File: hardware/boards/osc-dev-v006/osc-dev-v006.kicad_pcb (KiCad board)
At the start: 4 copper layers, 60 x 60 mm, 93 parts, among them J1 JST-PH-H, J10 PIN-1-3P, J11 JST-PH-V, J2 TERM, J3 PIN-1-3P, J4 PIN-2-3P, J5 JST-ZH-H, J6 PIN-1-2P, J7 PIN-1-5P, J8 PIN-2-2P, J9 PIN-1-3P, U1 HT7533-1, U2 DRV8212PDSGR, U3 CH32V006F8P6, U4 74LVC2G241

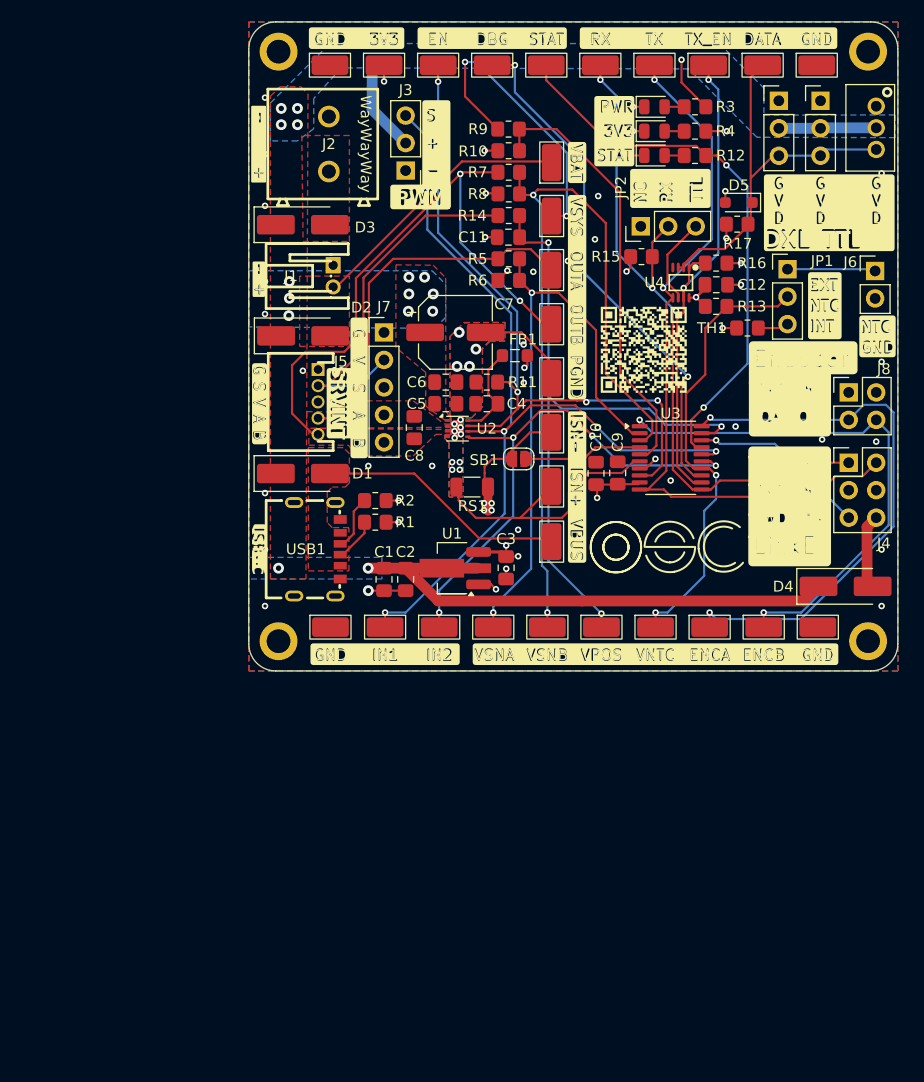
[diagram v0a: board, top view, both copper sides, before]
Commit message: hw: osc-dev-v006 rev-2a - 6l precision respin, direct-wire bus, docs
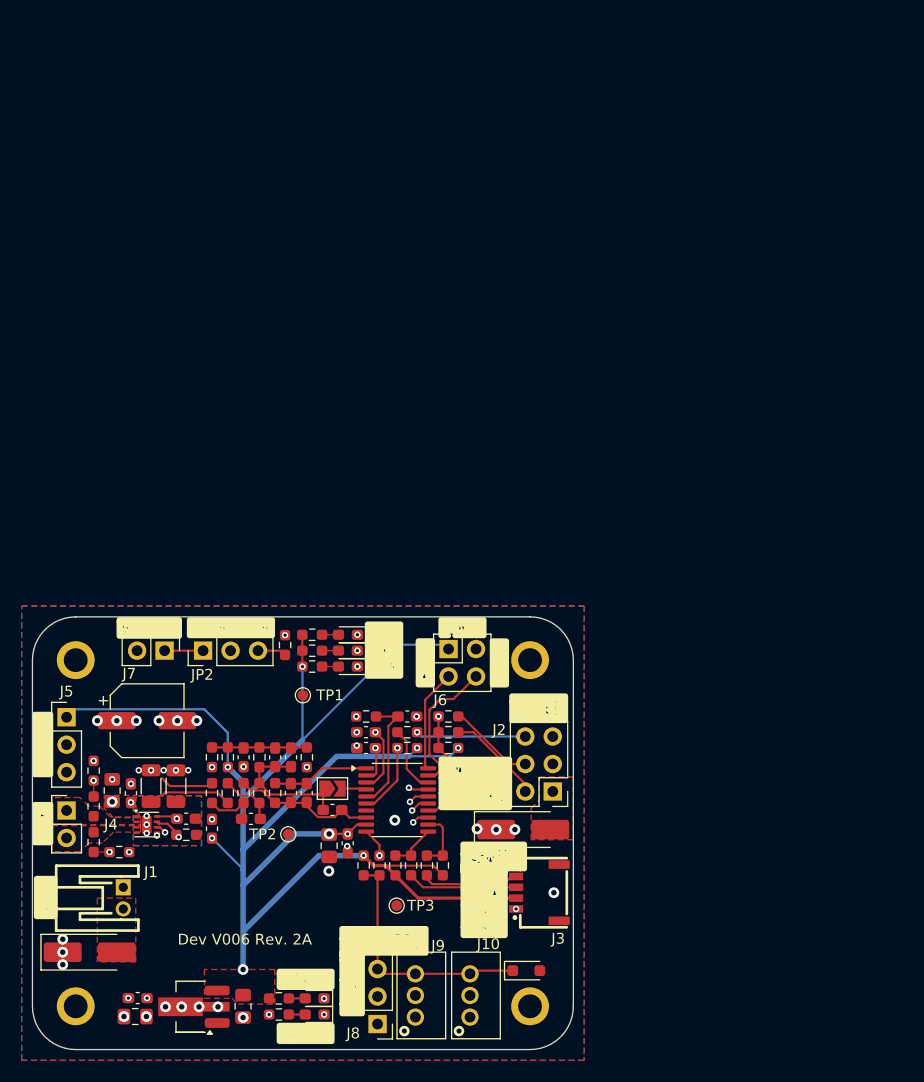
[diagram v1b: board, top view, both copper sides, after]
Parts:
- removed C10, C11, C12: 0.1µF, Capacitor_SMD:C_0805_2012Metric_Pad1.18x1.45mm_HandSolder
- removed J11: JST-PH-V, shared:CONN-TH_B3B-PH-K-S
- removed LED3: RED, LED_SMD:LED_0805_2012Metric
- removed R15, R16, R17: 10kΩ, Resistor_SMD:R_0805_2012Metric_Pad1.20x1.40mm_HandSolder
- removed SB1: Bootstrap, Jumper:SolderJumper-2_P1.3mm_Open_RoundedPad1.0x1.5mm
- removed TP10, TP11, TP12, TP13, TP14, TP15, TP16, TP17, TP18, TP19, TP20, TP21, TP22, TP23, TP24, TP25, TP26, TP27, TP28, TP4, TP5, TP6, TP7, TP8, TP9: TestPoint_Probe, TestPoint:TestPoint_Keystone_5015_Micro_Mini
- removed U4: 74LVC2G241, shared:VSSOP-8_L2.3-W2.0-P0.50-LS3.1-BR
- removed USB1: TYPE-C-H, shared:TYPE-C-SMD_TYPE-C-6P-073
- added C13: 100nF, Capacitor_SMD:C_0603_1608Metric_Pad1.08x0.95mm_HandSolder, F.Cu at (144.7, 119.2)
- added Cc1: 22pF, Capacitor_SMD:C_0603_1608Metric_Pad1.08x0.95mm_HandSolder, F.Cu at (132.4, 123.0)
- added Cc2: 22pF, Capacitor_SMD:C_0603_1608Metric_Pad1.08x0.95mm_HandSolder, F.Cu at (133.9, 126.3)
- added Cc3: 47pF, Capacitor_SMD:C_0603_1608Metric_Pad1.08x0.95mm_HandSolder, F.Cu at (133.9, 123.0)
- added Cc4: 47pF, Capacitor_SMD:C_0603_1608Metric_Pad1.08x0.95mm_HandSolder, F.Cu at (135.4, 126.3)
- added Cd1: 100nF, Capacitor_SMD:C_0603_1608Metric_Pad1.08x0.95mm_HandSolder, F.Cu at (129.5, 123.0)
- added Cin1: 100pF, Capacitor_SMD:C_0603_1608Metric_Pad1.08x0.95mm_HandSolder, F.Cu at (137.7, 127.8)
- added Ck1: 100pF, Capacitor_SMD:C_0603_1608Metric_Pad1.08x0.95mm_HandSolder, F.Cu at (130.2, 128.7)
- added Cv1: 100pF, Capacitor_SMD:C_0603_1608Metric_Pad1.08x0.95mm_HandSolder, F.Cu at (140.8, 122.1)
- added Cv2: 100pF, Capacitor_SMD:C_0603_1608Metric_Pad1.08x0.95mm_HandSolder, F.Cu at (140.8, 120.7)
- added D6: PESD5V0L1BA, Diode_SMD:D_SOD-323_HandSoldering, F.Cu at (155.7, 142.7)
- added LOGO1: osc-logo, shared:osc, F.Cu at (129.7, 136.1)
- added R21: 4K7, Resistor_SMD:R_0603_1608Metric_Pad0.98x0.95mm_HandSolder, F.Cu at (140.8, 119.2)
- added R22: 10K, Resistor_SMD:R_0603_1608Metric_Pad0.98x0.95mm_HandSolder, F.Cu at (144.7, 122.1)
- added R23: 33, Resistor_SMD:R_0603_1608Metric_Pad0.98x0.95mm_HandSolder, F.Cu at (142.1, 133.0)
- added R24: 10K, Resistor_SMD:R_0603_1608Metric_Pad0.98x0.95mm_HandSolder, F.Cu at (140.6, 133.0)
- added RS2: 60m, Resistor_SMD:R_1206_3216Metric, F.Cu at (123.3, 125.6)
- added Rd1: 1K6, Resistor_SMD:R_0603_1608Metric_Pad0.98x0.95mm_HandSolder, F.Cu at (128.1, 123.0)
- added Rd2: 300, Resistor_SMD:R_0603_1608Metric_Pad0.98x0.95mm_HandSolder, F.Cu at (126.6, 123.0)
- added Rd3: 300, Resistor_SMD:R_0603_1608Metric_Pad0.98x0.95mm_HandSolder, F.Cu at (135.4, 123.0)
- added Rf1: 6K4, Resistor_SMD:R_0603_1608Metric_Pad0.98x0.95mm_HandSolder, F.Cu at (131.0, 123.0)
- added Rf2: 6K4, Resistor_SMD:R_0603_1608Metric_Pad0.98x0.95mm_HandSolder, F.Cu at (132.4, 126.3)
- added Rg1: 430, Resistor_SMD:R_0603_1608Metric_Pad0.98x0.95mm_HandSolder, F.Cu at (131.0, 126.3)
- added Rg2: 430, Resistor_SMD:R_0603_1608Metric_Pad0.98x0.95mm_HandSolder, F.Cu at (129.5, 126.3)
- added Rk1: 0, Resistor_SMD:R_0603_1608Metric_Pad0.98x0.95mm_HandSolder, F.Cu at (128.1, 126.3)
- added Rk2: 0, Resistor_SMD:R_0603_1608Metric_Pad0.98x0.95mm_HandSolder, F.Cu at (126.6, 126.3)
- added Rv1: 20K, Resistor_SMD:R_0603_1608Metric_Pad0.98x0.95mm_HandSolder, F.Cu at (115.7, 127.5)
- added Rv2: 10K, Resistor_SMD:R_0603_1608Metric_Pad0.98x0.95mm_HandSolder, F.Cu at (115.7, 124.2)
- added Rv3: 20K, Resistor_SMD:R_0603_1608Metric_Pad0.98x0.95mm_HandSolder, F.Cu at (115.7, 130.8)
- added Rv4: 10K, Resistor_SMD:R_0603_1608Metric_Pad0.98x0.95mm_HandSolder, F.Cu at (118.0, 131.7)
- C2: footprint Capacitor_SMD:C_0805_2012Metric_Pad1.18x1.45mm_HandSolder -> Capacitor_SMD:C_0603_1608Metric_Pad1.08x0.95mm_HandSolder
- C4, C8: value 0.1µF -> 10µF
- C5: value 0.1µF -> 100nF; footprint Capacitor_SMD:C_0805_2012Metric_Pad1.18x1.45mm_HandSolder -> Capacitor_SMD:C_0603_1608Metric_Pad1.08x0.95mm_HandSolder
- C6: value 10µF -> 100nF; footprint Capacitor_SMD:C_0805_2012Metric_Pad1.18x1.45mm_HandSolder -> Capacitor_SMD:C_0603_1608Metric_Pad1.08x0.95mm_HandSolder
- C7: value 100µF -> 100nF; footprint Capacitor_SMD:CP_Elec_6.3x5.4 -> Capacitor_SMD:C_0603_1608Metric_Pad1.08x0.95mm_HandSolder
- C9: value 10µF -> 100µF; footprint Capacitor_SMD:C_0805_2012Metric_Pad1.18x1.45mm_HandSolder -> Capacitor_SMD:CP_Elec_6.3x5.4
- D3, D4: value SS54 -> BLUE; footprint Diode_SMD:D_SMA_Handsoldering -> LED_SMD:LED_0603_1608Metric_Pad1.05x0.95mm_HandSolder
- D5: value PESD5V0L1BA -> RED; footprint Diode_SMD:D_SOD-323_HandSoldering -> LED_SMD:LED_0603_1608Metric_Pad1.05x0.95mm_HandSolder
- FB1: footprint Inductor_SMD:L_0805_2012Metric_Pad1.05x1.20mm_HandSolder -> Inductor_SMD:L_0603_1608Metric_Pad1.05x0.95mm_HandSolder
- J10, J9: value PIN-1-3P -> TTL-JST; footprint Connector_PinHeader_2.54mm:PinHeader_1x03_P2.54mm_Vertical -> shared:CONN-TH_B3B-PH-K-S
- J2: value TERM -> LINKE; footprint shared:CONN-TH_2P-P5.00_WJ500V-5.08-2P -> Connector_PinHeader_2.54mm:PinHeader_2x03_P2.54mm_Vertical
- J3: value PIN-1-3P -> Qwiic; footprint Connector_PinHeader_2.54mm:PinHeader_1x03_P2.54mm_Vertical -> shared:CONN-SMD_SH1.0MM-4P-WT
- J4: value PIN-2-3P -> MOT; footprint Connector_PinHeader_2.54mm:PinHeader_2x03_P2.54mm_Vertical -> Connector_PinHeader_2.54mm:PinHeader_1x02_P2.54mm_Vertical
- J5: value JST-ZH-H -> POS; footprint shared:CONN-TH_S5B-ZR-LF-SN -> Connector_PinHeader_2.54mm:PinHeader_1x03_P2.54mm_Vertical
- J6: value PIN-1-2P -> ENC; footprint Connector_PinHeader_2.54mm:PinHeader_1x02_P2.54mm_Vertical -> Connector_PinHeader_2.54mm:PinHeader_2x02_P2.54mm_Vertical
- J7: value PIN-1-5P -> NTC; footprint Connector_PinHeader_2.54mm:PinHeader_1x05_P2.54mm_Vertical -> Connector_PinHeader_2.54mm:PinHeader_1x02_P2.54mm_Vertical
- J8: value PIN-2-2P -> TTL; footprint Connector_PinHeader_2.54mm:PinHeader_2x02_P2.54mm_Vertical -> Connector_PinHeader_2.54mm:PinHeader_1x03_P2.54mm_Vertical
- JP1: value JP-3 -> BOOTSTRAP; footprint Connector_PinHeader_2.54mm:PinHeader_1x03_P2.54mm_Vertical -> Jumper:SolderJumper-2_P1.3mm_Open_TrianglePad1.0x1.5mm
- LED1, LED2: footprint LED_SMD:LED_0805_2012Metric -> LED_SMD:LED_0603_1608Metric_Pad1.05x0.95mm_HandSolder
- R1: value 5.1kΩ -> 20K; footprint Resistor_SMD:R_0805_2012Metric_Pad1.20x1.40mm_HandSolder -> Resistor_SMD:R_0603_1608Metric_Pad0.98x0.95mm_HandSolder
- R10, R11: value 10kΩ -> 100; footprint Resistor_SMD:R_0805_2012Metric_Pad1.20x1.40mm_HandSolder -> Resistor_SMD:R_0603_1608Metric_Pad0.98x0.95mm_HandSolder
- R12: value 1kΩ -> 4K7; footprint Resistor_SMD:R_0805_2012Metric_Pad1.20x1.40mm_HandSolder -> Resistor_SMD:R_0603_1608Metric_Pad0.98x0.95mm_HandSolder
- R13, R8: value 10kΩ -> 4K7; footprint Resistor_SMD:R_0805_2012Metric_Pad1.20x1.40mm_HandSolder -> Resistor_SMD:R_0603_1608Metric_Pad0.98x0.95mm_HandSolder
- R14: value 4.7kΩ -> 10K; footprint Resistor_SMD:R_0805_2012Metric_Pad1.20x1.40mm_HandSolder -> Resistor_SMD:R_0603_1608Metric_Pad0.98x0.95mm_HandSolder
- R2: value 5.1kΩ -> 10K; footprint Resistor_SMD:R_0805_2012Metric_Pad1.20x1.40mm_HandSolder -> Resistor_SMD:R_0603_1608Metric_Pad0.98x0.95mm_HandSolder
- R3, R4: value 1.5kΩ -> 4K7; footprint Resistor_SMD:R_0805_2012Metric_Pad1.20x1.40mm_HandSolder -> Resistor_SMD:R_0603_1608Metric_Pad0.98x0.95mm_HandSolder
- R5, R7: value 20kΩ -> 100; footprint Resistor_SMD:R_0805_2012Metric_Pad1.20x1.40mm_HandSolder -> Resistor_SMD:R_0603_1608Metric_Pad0.98x0.95mm_HandSolder
- R6: value 10kΩ -> 1K; footprint Resistor_SMD:R_0805_2012Metric_Pad1.20x1.40mm_HandSolder -> Resistor_SMD:R_0603_1608Metric_Pad0.98x0.95mm_HandSolder
- R9: value 20kΩ -> 10K; footprint Resistor_SMD:R_0805_2012Metric_Pad1.20x1.40mm_HandSolder -> Resistor_SMD:R_0603_1608Metric_Pad0.98x0.95mm_HandSolder
- RS1: value 10mΩ 1% -> 33m
- TH1: footprint Resistor_SMD:R_0805_2012Metric_Pad1.20x1.40mm_HandSolder -> Resistor_SMD:R_0603_1608Metric_Pad0.98x0.95mm_HandSolder
- TP1, TP2, TP3: value TestPoint_Probe -> GND; footprint TestPoint:TestPoint_Keystone_5015_Micro_Mini -> TestPoint:TestPoint_Pad_D1.0mm
- U2: value DRV8212PDSGR -> CH32V006F8P6; footprint Package_SON:WSON-8-1EP_2x2mm_P0.5mm_EP0.9x1.6mm -> Package_SO:TSSOP-20_4.4x6.5mm_P0.65mm
- U3: value CH32V006F8P6 -> DRV8212PDSGR; footprint Package_SO:TSSOP-20_4.4x6.5mm_P0.65mm -> Package_SON:Texas_DSG0008A_WSON-8-1EP_2x2mm_P0.5mm_EP0.9x1.6mm
- moved H2 114.7 mm to (114.0, 146.0)
- moved LED1 89.6 mm to (136.1, 146.8), turned to 180 degrees
- moved J9 89.3 mm to (145.4, 145.0), turned to -90 degrees
- moved J10 88.8 mm to (150.4, 145.0), turned to -90 degrees
- moved LED2 86.1 mm to (136.1, 145.3), turned to 180 degrees
- moved J4 79.1 mm to (113.2, 127.9)
- moved J8 72.8 mm to (141.9, 147.6), turned to 180 degrees
- moved R12 69.6 mm to (147.9, 133.0), turned to -90 degrees
- moved J3 67.9 mm to (156.7, 135.5), turned to 90 degrees
- moved R10 66.5 mm to (146.5, 133.0), turned to -90 degrees
- moved R14 64.5 mm to (124.2, 130.1), turned to 0 degrees
- moved JP1 63.8 mm to (137.7, 125.9)
- moved J2 63.3 mm to (158.1, 126.1), turned to 180 degrees
- moved J1 60.7 mm to (118.4, 136.0)
- moved R3 60.3 mm to (135.9, 111.7), turned to 0 degrees
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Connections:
- C4 pad 1: /M_DRV/+3V3_DRV -> +3V3
- C4 pad 2: PGND -> GND
- C5 pad 1: VSYS -> +3V3
- C5 pad 2: PGND -> GND
- C6 pad 1: VSYS -> +3V3_DRV
- C7 pad 2: PGND -> GND
- C8 pad 1: /MOT_A -> VSYS
- C8 pad 2: /MOT_B -> GND
- C9 pad 1: +3V3 -> VSYS
- D1 pad 2: VBUS -> VBAT
- D2 pad 2: VBAT -> VPROG
- D3 pad 1: VSYS -> /MCU/TEL
- D3 pad 2: VEXT -> Net-(D3-A)
- D4 pad 1: VSYS -> /COMMS/DATA
- D4 pad 2: VPROG -> Net-(D4-A)
- D5 pad 1: /DATA -> /MCU/STAT
- D5 pad 2: GND -> Net-(D5-A)
- FB1 pad 2: /M_DRV/+3V3_DRV -> +3V3_DRV
- J10 pad 3: /DATA -> /COMMS/DATA_J
- J2 pad 1: VEXT -> VPROG
- J2 pad 2: GND -> /MCU/TEL_TX
- J3 pad 2: VSYS -> +3V3
- J3 pad 3: /IN1 -> /MCU/SDA_J
- J4 pad 1: /RX -> MOT_A
- J4 pad 2: /TX -> MOT_B
- J5 pad 1: GND -> +3V3
- J5 pad 2: /SERVO_IO/POT -> GND
- J5 pad 3: +3V3 -> /SENS/POT
- J6 pad 1: /SERVO_IO/VNTC_EXT -> +3V3
- J7 pad 1: GND -> /SENS/VNTC_EXT
- J7 pad 2: /SERVO_IO/POT -> GND
- J8 pad 1: +3V3 -> GND
- J8 pad 2: GND -> VSYS
- J8 pad 3: /ENCA -> /COMMS/DATA_J
- J9 pad 3: /DATA -> /COMMS/DATA_J
- JP1 pad 1: /SERVO_IO/VNTC_EXT -> /MCU/OPA_P
- JP1 pad 2: /VNTC -> /MCU/RST
- JP2 pad 1: unconnected-(JP2-A-Pad1) -> /SENS/VNTC_EXT
- JP2 pad 2: /RX -> /MCU/VNTC
- JP2 pad 3: /COMMS/JP_RX -> /SENS/VNTC_INT
- NT1 pad 1: /ISNS+ -> /SENS/ISNS_K+
- NT2 pad 1: /ISNS- -> /SENS/ISNS_K-
- R1 pad 1: GND -> VSYS
- R1 pad 2: /POWER/CC1 -> /POWER/LED_VSYS
- R10 pad 1: /VSNS -> /MCU/SCL
- R10 pad 2: GND -> /MCU/SCL_J
- R11 pad 1: /EN -> /MCU/SDA
- R11 pad 2: PGND -> /MCU/SDA_J
- R12 pad 1: /STAT -> /MCU/SCL
- R12 pad 2: Net-(LED3-A) -> +3V3
- R13 pad 1: +3V3 -> /MCU/SDA
- R13 pad 2: /VNTC -> +3V3
- R14 pad 1: /VPOS -> /DRV/DRV_EN
- R14 pad 2: /SERVO_IO/POT -> PGND
- R2 pad 1: GND -> +3V3
- R2 pad 2: /POWER/CC2 -> /POWER/LED_3V3
- R3 pad 1: VSYS -> +3V3
- R3 pad 2: /POWER/LED_VSYS -> Net-(D3-A)
- R4 pad 2: /POWER/LED_3V3 -> Net-(D4-A)
- R5 pad 1: /MOT_A -> /MCU/TEL
- R5 pad 2: /VSNA -> /MCU/TEL_TX
- R6 pad 1: /VSNA -> /MCU/TEL
- R6 pad 2: GND -> /MCU/TEL_RX
- R7 pad 1: /MOT_B -> /MCU/SWDIO
- R7 pad 2: /VSNB -> /MCU/SWDIO_J
- R8 pad 1: /VSNB -> +3V3
- R8 pad 2: GND -> Net-(D5-A)
- R9 pad 1: VSYS -> +3V3
- R9 pad 2: /VSNS -> /MCU/TEL
- TH1 pad 1: /SERVO_IO/VNTC_INT -> /SENS/VNTC_INT
- TP2 pad 1: /IN1 -> GND
- TP3 pad 1: /IN2 -> GND
- U2 pad 1: VSYS -> /MCU/OPA_OUT
- U2 pad 2: /MOT_A -> /MCU/VSNA
- U2 pad 3: /MOT_B -> /MCU/VSNB
- U2 pad 4: PGND -> /MCU/RST
- U2 pad 5: /IN2 -> /MCU/VPOS
- U2 pad 6: /IN1 -> /MCU/VNTC
- U2 pad 7: /EN -> GND
- U2 pad 8: /M_DRV/+3V3_DRV -> /MCU/OPA_N
- U2 pad 9: PGND -> +3V3
- U3 pad 1: /ENCB -> VSYS
- U3 pad 2: /VSNA -> MOT_A
- U3 pad 3: /VSNB -> MOT_B
- U3 pad 4: /MCU/OPN2 -> PGND
- U3 pad 5: /VSNS -> /DRV/DRV_IN2
- U3 pad 6: /ISNS+ -> /DRV/DRV_IN1
- U3 pad 7: GND -> /DRV/DRV_EN
- U3 pad 8: /EN -> +3V3_DRV
- U3 pad 9: +3V3 -> PGND
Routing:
- net +3V3: track 21.9 -> 153.4 mm
- net VSYS: track 100.3 -> 0.00 mm
- net /IN1: track 84.5 -> 0.00 mm, vias 4 -> 0
- net /VSNB: track 74.7 -> 0.00 mm, vias 2 -> 0
- net /TX: track 68.8 -> 0.00 mm, vias 2 -> 0
- net /RX: track 64.8 -> 0.00 mm, vias 3 -> 0
- net /EN: track 64.5 -> 0.00 mm, vias 4 -> 0
- net /VPOS: track 62.1 -> 0.00 mm, vias 3 -> 0
- net /MOT_B: track 55.1 -> 0.00 mm, vias 2 -> 0
- net /VSNA: track 55.0 -> 0.00 mm, vias 2 -> 0
- net /ENCA: track 51.7 -> 0.00 mm, vias 2 -> 0
- net /STAT: track 51.0 -> 0.00 mm, vias 2 -> 0
- net /ENCB: track 49.9 -> 0.00 mm, vias 2 -> 0
- net /DBG: track 48.1 -> 0.00 mm, vias 2 -> 0
- net /IN2: track 48.0 -> 0.00 mm, vias 4 -> 0
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- added copper zone on F.Cu, net +3V3
- added copper zone on In2.Cu, net GND
- added copper zone on In4.Cu, net GND
- added copper zone on F.Cu, net MOT_A
- added copper zone on F.Cu, net MOT_B
- added copper zone on F.Cu, net VPROG
- added copper zone on In3.Cu, net VSYS
- removed copper zone on In2.Cu, net +3V3
- removed copper zone on F.Cu, net /MOT_A
- removed copper zone on F.Cu, net /MOT_B
- removed copper zone on In1.Cu, net PGND
- removed copper zone on In2.Cu, net PGND
- removed copper zone on F.Cu, net VBUS
- removed copper zone on F.Cu, net VEXT
- removed copper zone on B.Cu, net VSYS
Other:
- board size 60 x 60 mm -> 50 x 40 mm
- copper layers 4 -> 6
- board text added: "- +"
- board text added: "3"
- board text added: "3 G P"
- board text added: "A B"
- board text added: "D"
- board text added: "DAT"
- board text added: "Dev V006 Rev. 2A"
- board text added: "ENC"
- board text added: "EX"
- board text added: "IN"
- board text added: "NTC_EX"
- board text added: "OSC Dev V006 Rev. 2A"
- board text added: "OSC TTL"
- board text added: "Qwiic"
- board text added: "SCL"
- board text added: "SDA"
- board text added: "STA"
- board text added: "TEL"
- board text removed: "+"
- board text removed: "-"
- board text removed: "D3"
- board text removed: "DATA"
- board text removed: "DBG"
- board text removed: "DXL TTL"
- board text removed: "EN"
- board text removed: "ENCA"
- board text removed: "ENCB"
- board text removed: "EXT"
- board text removed: "Encoder"
- board text removed: "G V D"
- board text removed: "IN1"
- board text removed: "IN2"
- board text removed: "INT"
- board text removed: "ISN+"
- board text removed: "ISN-"
- board text removed: "JST-PH 2P"
- board text removed: "JST-ZH 5P"
- board text removed: "NC"
- board text removed: "OSC Dev V006 Rev. B"
- board text removed: "OUTA"
- board text removed: "OUTB"
- board text removed: "PGND"
- board text removed: "PWM"
- board text removed: "PWR"
- board text removed: "QA"
- board text removed: "QB"
- board text removed: "S"
- board text removed: "SCREW TERM"
- board text removed: "SRVINT"
- board text removed: "STAT"
- board text removed: "TTL"
- board text removed: "TX_EN"
- board text removed: "USB-C"
- board text removed: "USB-C PWR"
- board text removed: "VBAT"
- board text removed: "VBUS"
- board text removed: "VNTC"
- board text removed: "VPOS"
- board text removed: "VSNA"
- board text removed: "VSNB"
- board text removed: "WayWayWay"
